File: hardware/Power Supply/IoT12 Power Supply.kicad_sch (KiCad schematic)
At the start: 33 parts, among them J1 Screw_Terminal_01x03, J2 JST B2B-XH-A, J3 JST B4B-XH-A, K1 Omron G5LE-1 24VDC, Q1 MMBT2222, U1 LM2596S-ADJ

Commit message: Add PDF. Enlarge F1 pad size.
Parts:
- F1: footprint Varistor:RV_Disc_D9mm_W3.3mm_P5mm -> Varistor-extra:RV_Disc_D9mm_W3.3mm_P5mm
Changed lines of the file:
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@@
     (property "Reference" "F1" (id 0) (at 39.37 31.75 90))
     (property "Value" "PTC 1.5A/30V" (id 1) (at 39.37 34.29 90))
-    (property "Footprint" "Varistor:RV_Disc_D9mm_W3.3mm_P5mm" (id 2) (at 34.29 39.37 0)
+    (property "Footprint" "Varistor-extra:RV_Disc_D9mm_W3.3mm_P5mm" (id 2) (at 34.29 39.37 0)
       (effects (font (size 1.27 1.27)) (justify left) hide)
     )
@@
     )
     (path "/b5b2ae0c-b2cd-4fd8-9072-13fbf68a05b9"
-      (reference "F1") (unit 1) (value "PTC 1.5A/30V") (footprint "Varistor:RV_Disc_D9mm_W3.3mm_P5mm")
+      (reference "F1") (unit 1) (value "PTC 1.5A/30V") (footprint "Varistor-extra:RV_Disc_D9mm_W3.3mm_P5mm")
     )
     (path "/2e41f05f-9743-469f-9aba-9201a232c639"

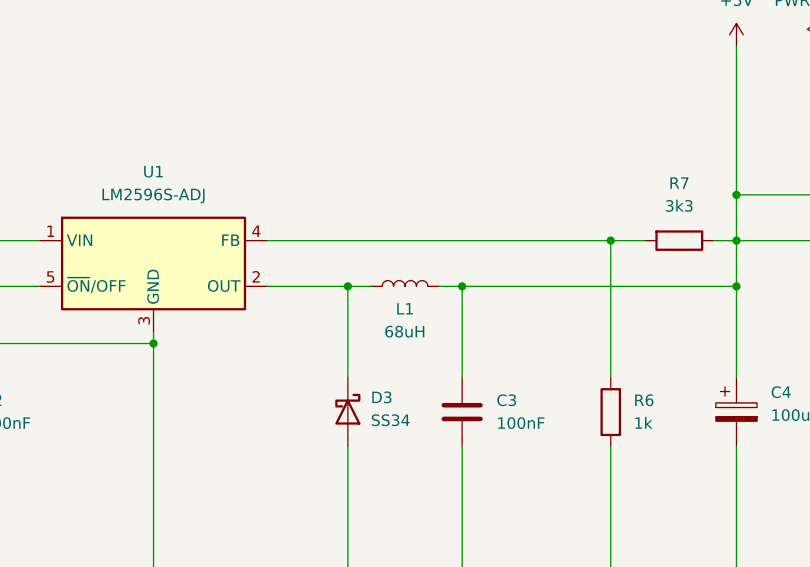
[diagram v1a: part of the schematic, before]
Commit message: Update Power Supply project to Kicad 7.0.2
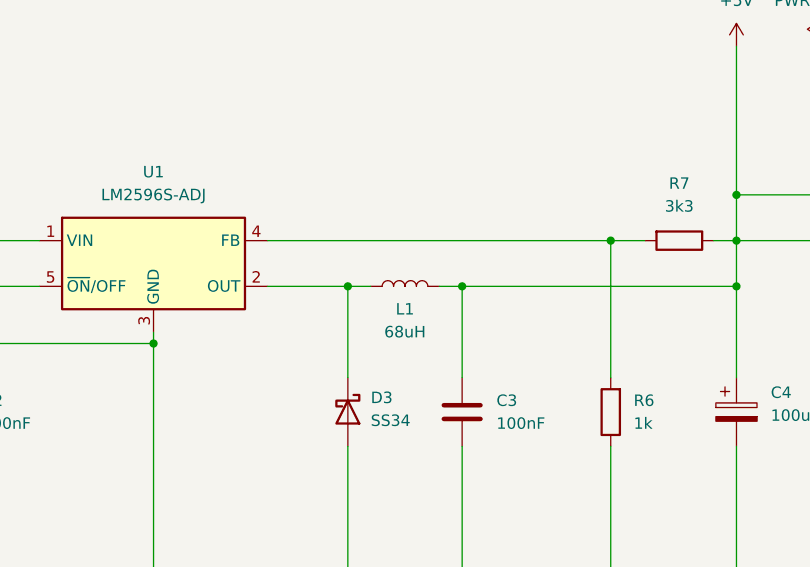
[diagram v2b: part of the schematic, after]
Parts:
- J2: symbol Connector:Conn_01x02_Male -> Connector:Conn_01x02_Pin
- J3: symbol Connector:Conn_01x04_Male -> Connector:Conn_01x04_Pin
- K1: footprint Relay_THT-fixed:Relay_SPDT_Omron-G5LE-1 -> Relay_THT:Relay_SPDT_Omron-G5LE-1
